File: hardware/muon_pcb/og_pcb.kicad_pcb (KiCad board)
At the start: 4 copper layers, 88 x 94.5 mm, 72 parts, among them J1 Conn_Coaxial, J12 USB_B_Micro, J2 Conn_Coaxial, J3 Conn_02x02_Top_Bottom, J4 Micro_SD_Card_Det1, J5 Conn_01x02_Pin, J6 Conn_Coaxial, SW4 SW_Push_Shielded, SW5 SW_Push_Shielded, U1 CD-PA1616D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

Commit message: uploaded pcb with gps 1pps implemented and cygnet logo
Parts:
- added G***: LOGO, 1my_footprints:cadence_cygnet_logo_placeholder, F.Cu at (129.7, 77.5)
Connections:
- U1 pad 13: unconnected-(U1-1PPS-Pad13) -> GPS 1PPS
- U12 pad 28: RF DIO4 -> RF DIO0
- U12 pad 29: unconnected-(U12-GPIO18-Pad29) -> RF DIO4
- U12 pad 40: unconnected-(U12-GPIO28_ADC2-Pad40) -> GPS 1PPS
- U16 pad 6: unconnected-(U16-DI/O0-Pad6) -> RF DIO0
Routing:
- net GPS 1PPS: track 0.00 -> 54.7 mm, vias 0 -> 4
- net RF DIO0: track 0.00 -> 32.1 mm, vias 0 -> 4
- removed copper zone on F.Cu, net (none)

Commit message: uploaded cleaner schematic
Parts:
- moved J4 31.9 mm to (128.4, 165.6), turned to 180 degrees
- moved C15 28.9 mm to (131.6, 162.7), turned to 0 degrees
- moved R12 23.4 mm to (146.7, 122.8), turned to 0 degrees
- moved U13 16.2 mm to (147.3, 129.8), turned to 90 degrees
- moved R7 14.3 mm to (125.1, 146.9), turned to 180 degrees
- moved C16 13.3 mm to (143.5, 126.9), turned to 180 degrees
- moved R13 10.6 mm to (129.3, 108.7), turned to 180 degrees
- moved BT1 9.30 mm to (164.1, 135.5), turned to 90 degrees
- moved FL1 7.62 mm to (141.7, 123.6)
- moved TP4 2.32 mm to (101.5, 111.8)
- moved C22 2.20 mm to (104.1, 134.8)
- moved C20 2.12 mm to (145.1, 118.5), turned to 180 degrees
- moved C21 1.75 mm to (153.7, 119.5)
- moved C12 1.74 mm to (132.3, 123.2)
- moved TP3 1.43 mm to (142.9, 115.5)
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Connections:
- net GPS UART Rx renamed MCU UART Tx
- net GPS UART Tx renamed MCU UART Rx
- C16 pad 1: +3.3V -> VCC Processed
- C19 pad 1: +3.3V -> GPS VCC
- C20 pad 1: +3.3V -> GPS VCC
- FL1 pad 1: Net-(U1-VCC) -> VCC Processed
- R12 pad 1: +3.3V -> VCC Processed
- R12 pad 2: GND -> GPS VCC
- R14 pad 1: Net-(U1-VCC) -> GPS VCC
- TP3 pad 1: Net-(U1-VCC) -> GPS VCC
- U1 pad 1: Net-(U1-VCC) -> GPS VCC
- U12 pad 35: RF Reset -> RF MOSI
- U12 pad 39: RF MOSI -> RF Reset
- U13 pad 7: GND -> GPS VCC
- U13 pad 8: +3.3V -> VCC Processed
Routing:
- net VBUS: track 79.7 -> 3.79 mm
- net GPS VCC: track 0.00 -> 24.3 mm
- net MicroSD CS: track 18.1 -> 42.2 mm, vias 0 -> 2
- net MicroSD MISO: track 15.8 -> 39.2 mm, vias 2 -> 0
- net MicroSD CLK: track 15.2 -> 38.6 mm
- net MicroSD MOSI: track 16.3 -> 39.0 mm, vias 2 -> 0
- net SCL1: track 13.5 -> 34.6 mm
- net SDA1: track 12.8 -> 30.9 mm
- net +3.3V: track 17.8 -> 32.3 mm, vias 29 -> 44
- net Net-(U1-VCC): track 10.8 -> 0.00 mm
- net RF Reset: track 43.9 -> 34.5 mm
- net GND: track 143.4 -> 134.2 mm, vias 66 -> 72
- net VCC Processed: track 0.00 -> 8.83 mm
- net /Sensors/VBACKUP: track 47.2 -> 55.0 mm
- net RP2040 Reset: track 39.1 -> 34.4 mm, vias 2 -> 1
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- added copper zone on F.Cu, net GND
- added copper zone on F.Cu, net VBUS

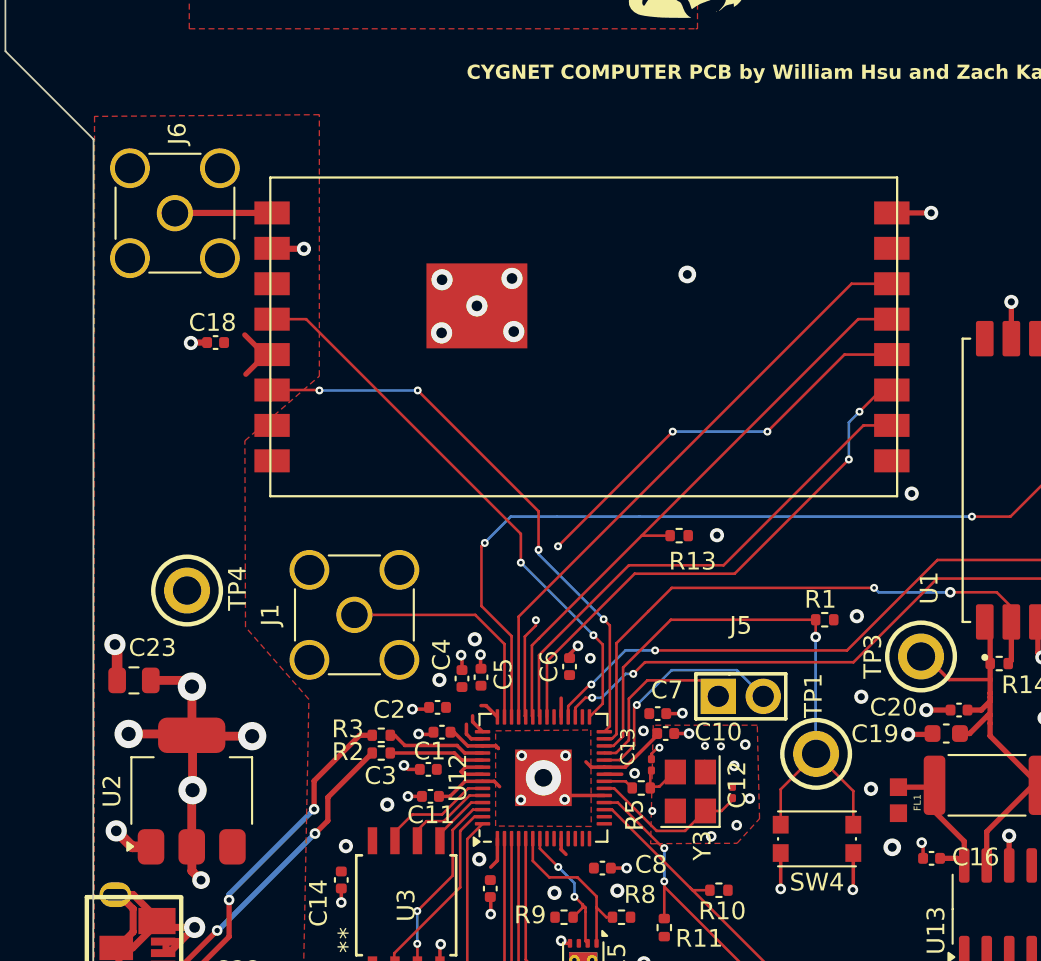
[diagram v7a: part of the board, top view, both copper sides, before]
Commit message: cleaned up schematic & implemented changes to layout
to do (off top of my head rn):
-organize project files
-verify design
-maybe check if schematic can be improved again

issues addressed from mikefly's comments:
- ina219 power monitor
- 5v vbus pour near microusb
-gnd pour around crystal oscillator
-removed mounting hole to gnd connection
- corrected microSD orientation and connections
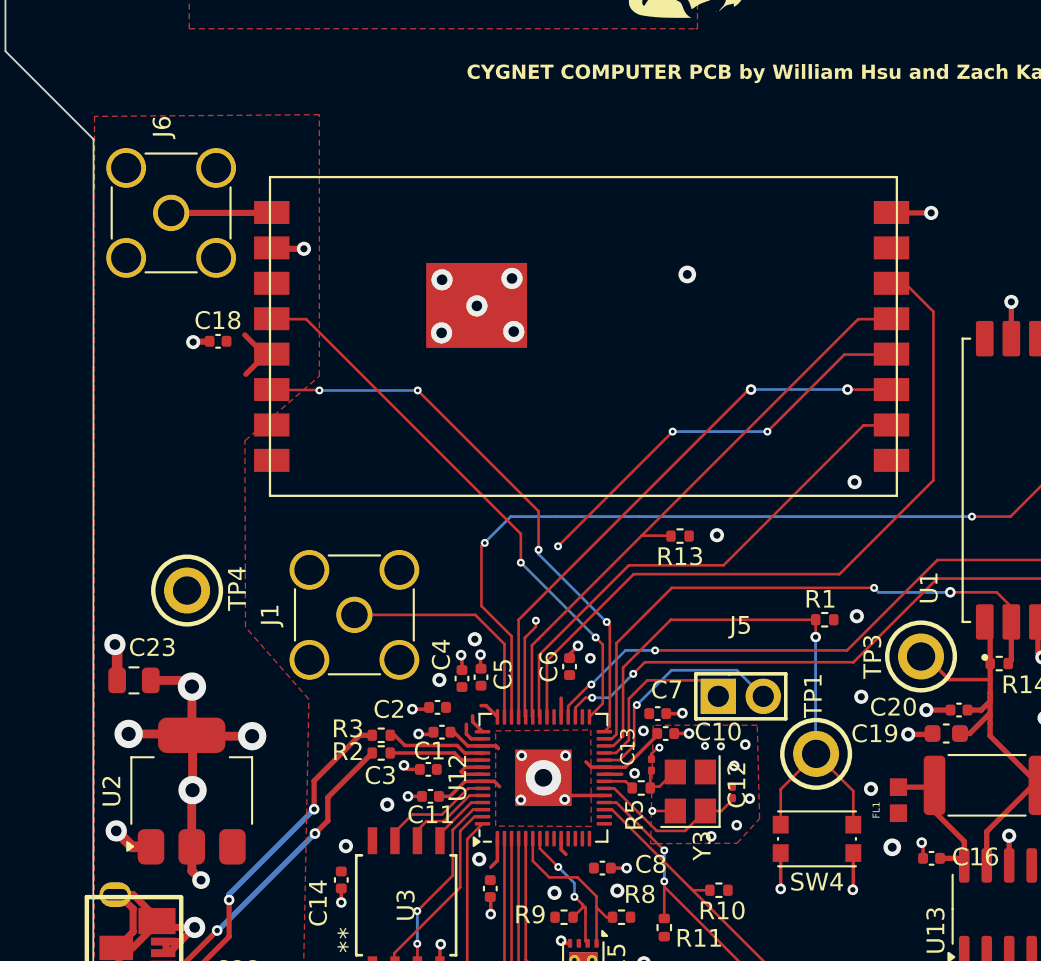
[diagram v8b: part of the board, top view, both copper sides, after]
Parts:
- moved J6 0.22 mm to (100.6, 90.5)
- moved C18 0.16 mm to (103.2, 97.7)
- moved R13 0.06 mm to (129.3, 108.7)
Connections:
- U12 pad 35: RF MOSI -> RF Reset
- U12 pad 39: RF Reset -> RF MOSI
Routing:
- net RF Reset: track 34.5 -> 41.8 mm
- net RF MOSI: track 30.3 -> 32.0 mm
- net GND: track 134.2 -> 135.5 mm
